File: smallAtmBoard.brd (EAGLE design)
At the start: 66.1 x 51.7 mm, 23 parts, among them IC1 ATMEGA-328P, IC2 7805, Y1 16MHz

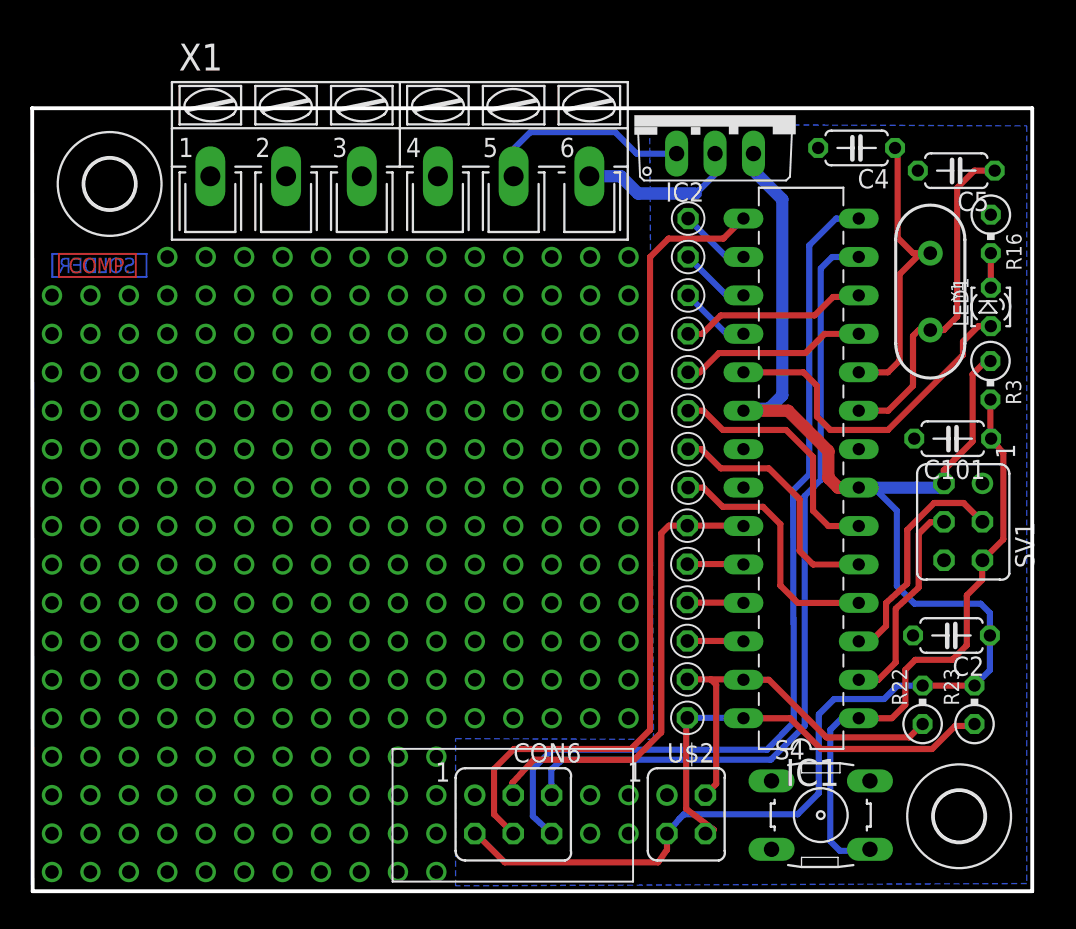
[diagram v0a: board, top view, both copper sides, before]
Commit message: remove i2c socket
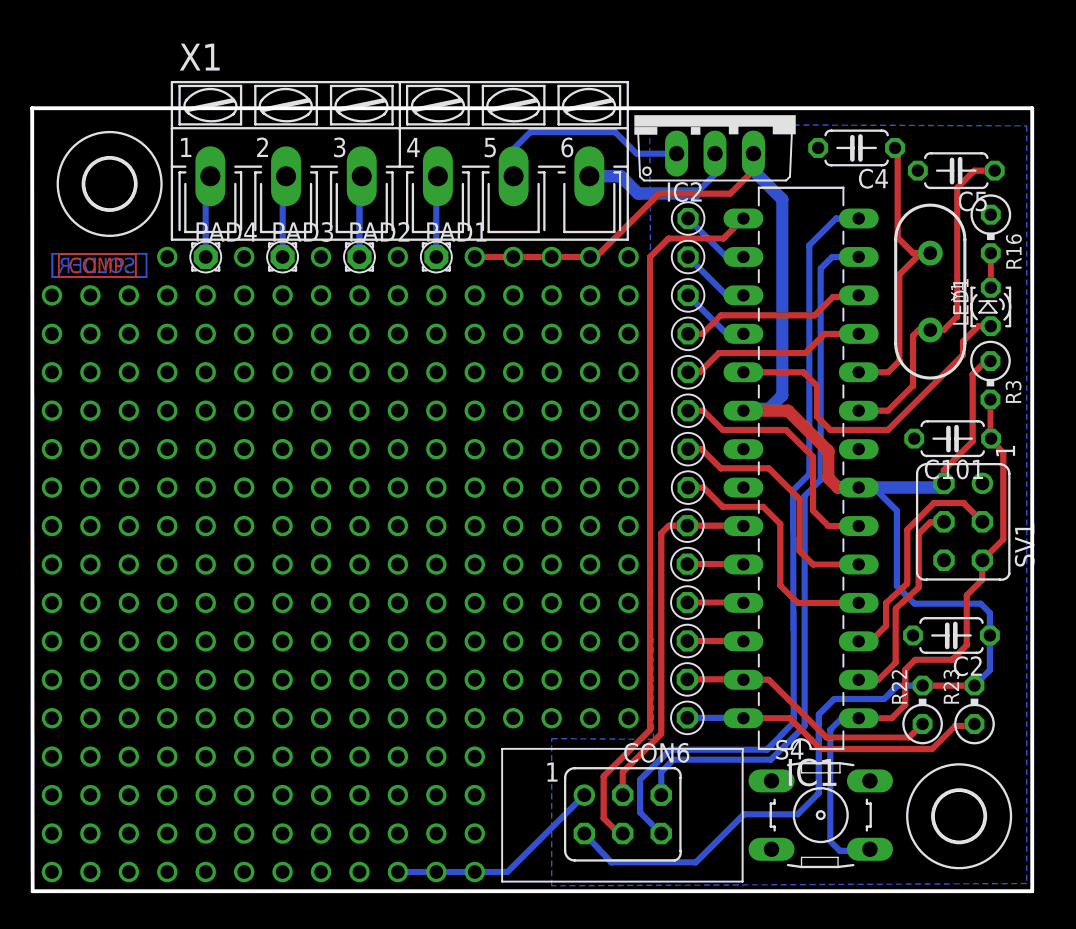
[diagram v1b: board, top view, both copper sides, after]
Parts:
- removed U$2: FE02-2, bauteile_jbt:FE02-2RAW
- added PAD1, PAD2, PAD3, PAD4: (no value), bauteile_jbt:PAD1,6/0,8
- moved CON6 7.24 mm to (39.0, 5.08)
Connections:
- new net N$115: PAD1.1, X1.4
- new net N$119: PAD2.1, X1.3
- new net N$123: PAD3.1, X1.2
- new net N$175: PAD4.1, X1.1
- net AT-A4/SDA: no longer U$2.3
- net AT-A5/SCL: no longer U$2.4
- net GND: no longer U$2.1
- net VCC: no longer U$2.2
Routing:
- net GND: track 10.7 -> 25.1 mm, vias 0 -> 3
- net VCC: track 107.7 -> 121.6 mm, vias 0 -> 4
- net AT-A5/SCL: track 29.4 -> 20.9 mm
- net AT-A4/SDA: track 25.6 -> 17.5 mm
- net AT-PD8: track 59.3 -> 51.8 mm
- net AT-PD9: track 54.6 -> 47.3 mm
- net AT-PD7: track 53.1 -> 45.8 mm
- net AT-A0: track 30.9 -> 24.0 mm
- net N$175: track 0.00 -> 5.46 mm, vias 1 -> 0
- net N$123: track 0.00 -> 5.43 mm, vias 1 -> 0
- net N$119: track 0.00 -> 5.40 mm, vias 1 -> 0
- net N$115: track 0.00 -> 5.38 mm, vias 1 -> 0
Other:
- board text added: "-"
- board text removed: "I2C"
- board text removed: "VCC"

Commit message: turn around connector for lcd and kbd
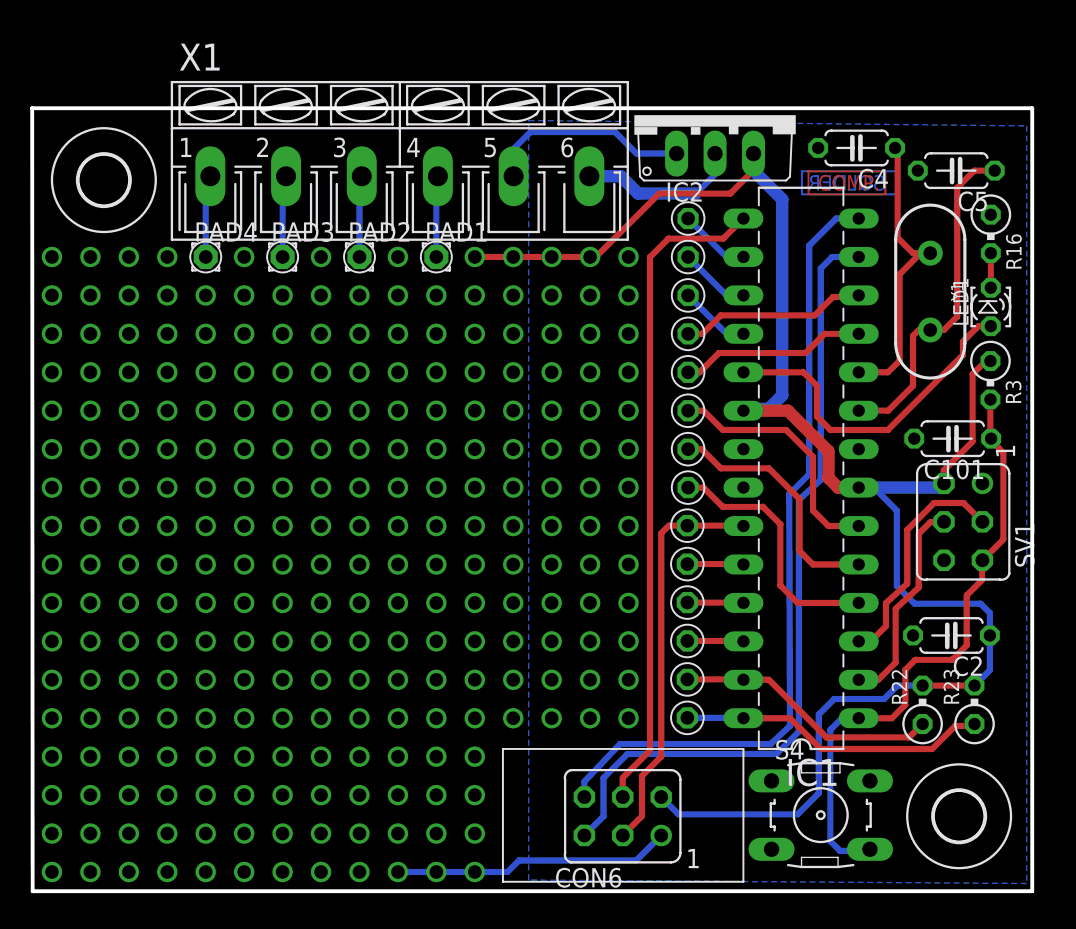
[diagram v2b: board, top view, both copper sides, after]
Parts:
- moved U$6 49.8 mm to (54.1, 46.8)
- moved U$7 49.8 mm to (53.7, 46.8)
- moved U$3 0.46 mm to (4.70, 47.0)
- moved CON6 0.13 mm to (39.0, 4.95), turned to 180 degrees
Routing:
- net AT-PD7: track 45.8 -> 52.6 mm
- net VCC: track 121.6 -> 114.9 mm
- net GND: track 25.1 -> 29.1 mm
- net AT-PD9: track 47.3 -> 43.7 mm
- net AT-A0: track 24.0 -> 26.7 mm
- net AT-PD8: track 51.8 -> 52.5 mm
